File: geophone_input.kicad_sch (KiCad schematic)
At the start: 6 parts, among them J4 Conn_01x03_Socket

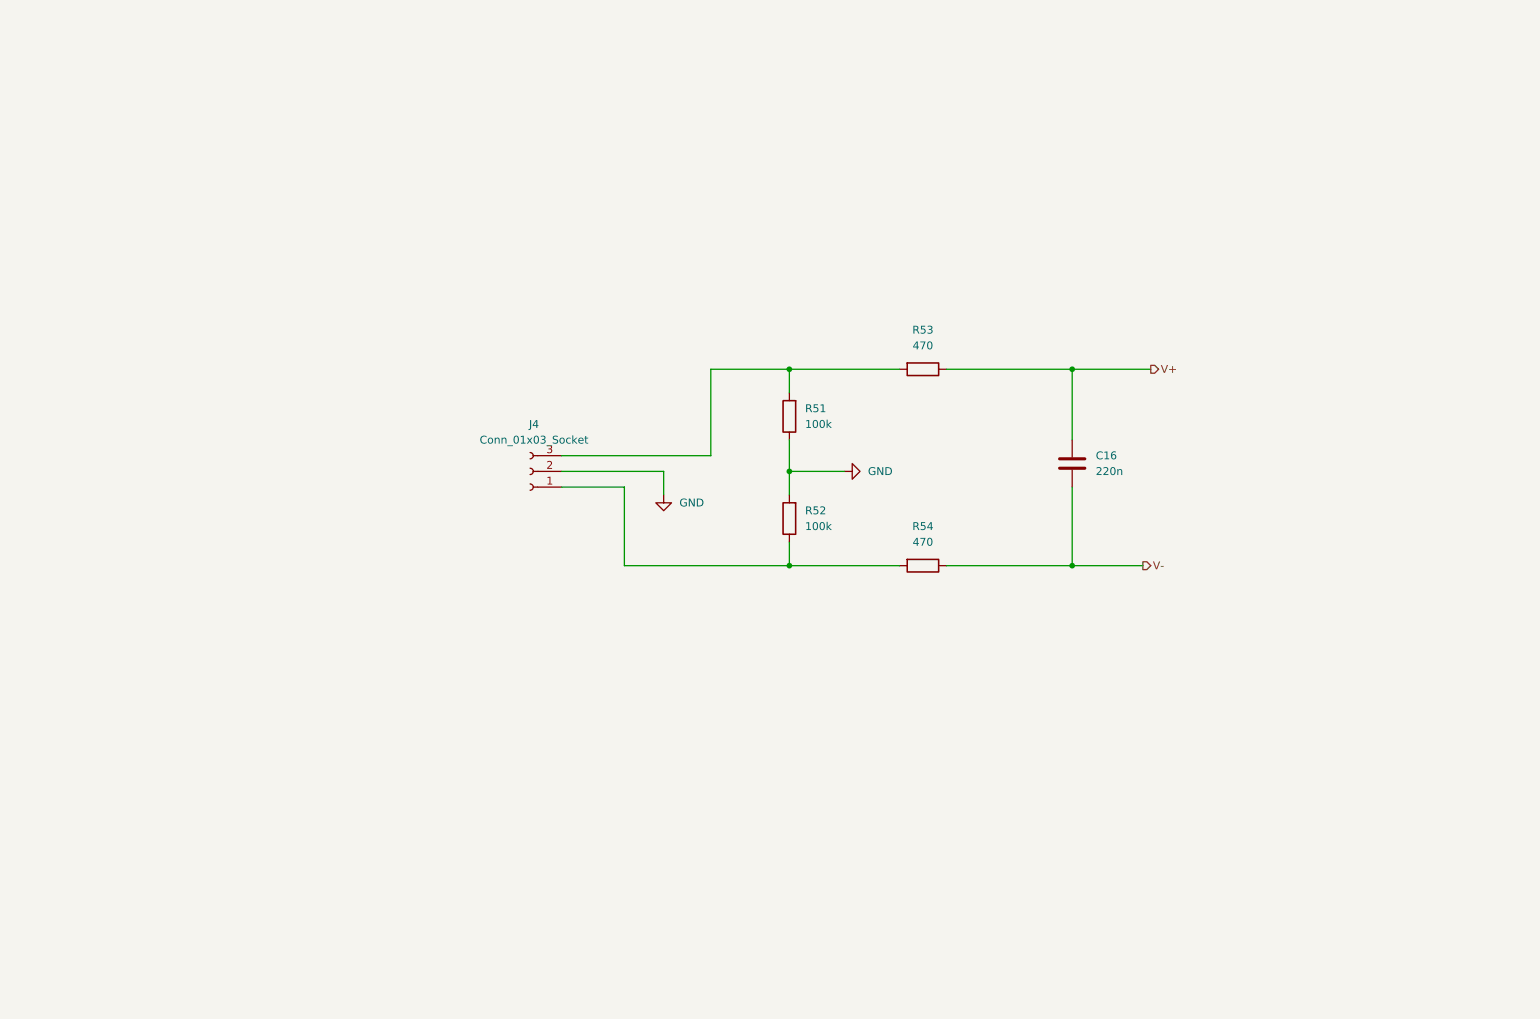
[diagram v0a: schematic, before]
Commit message: Active input filter
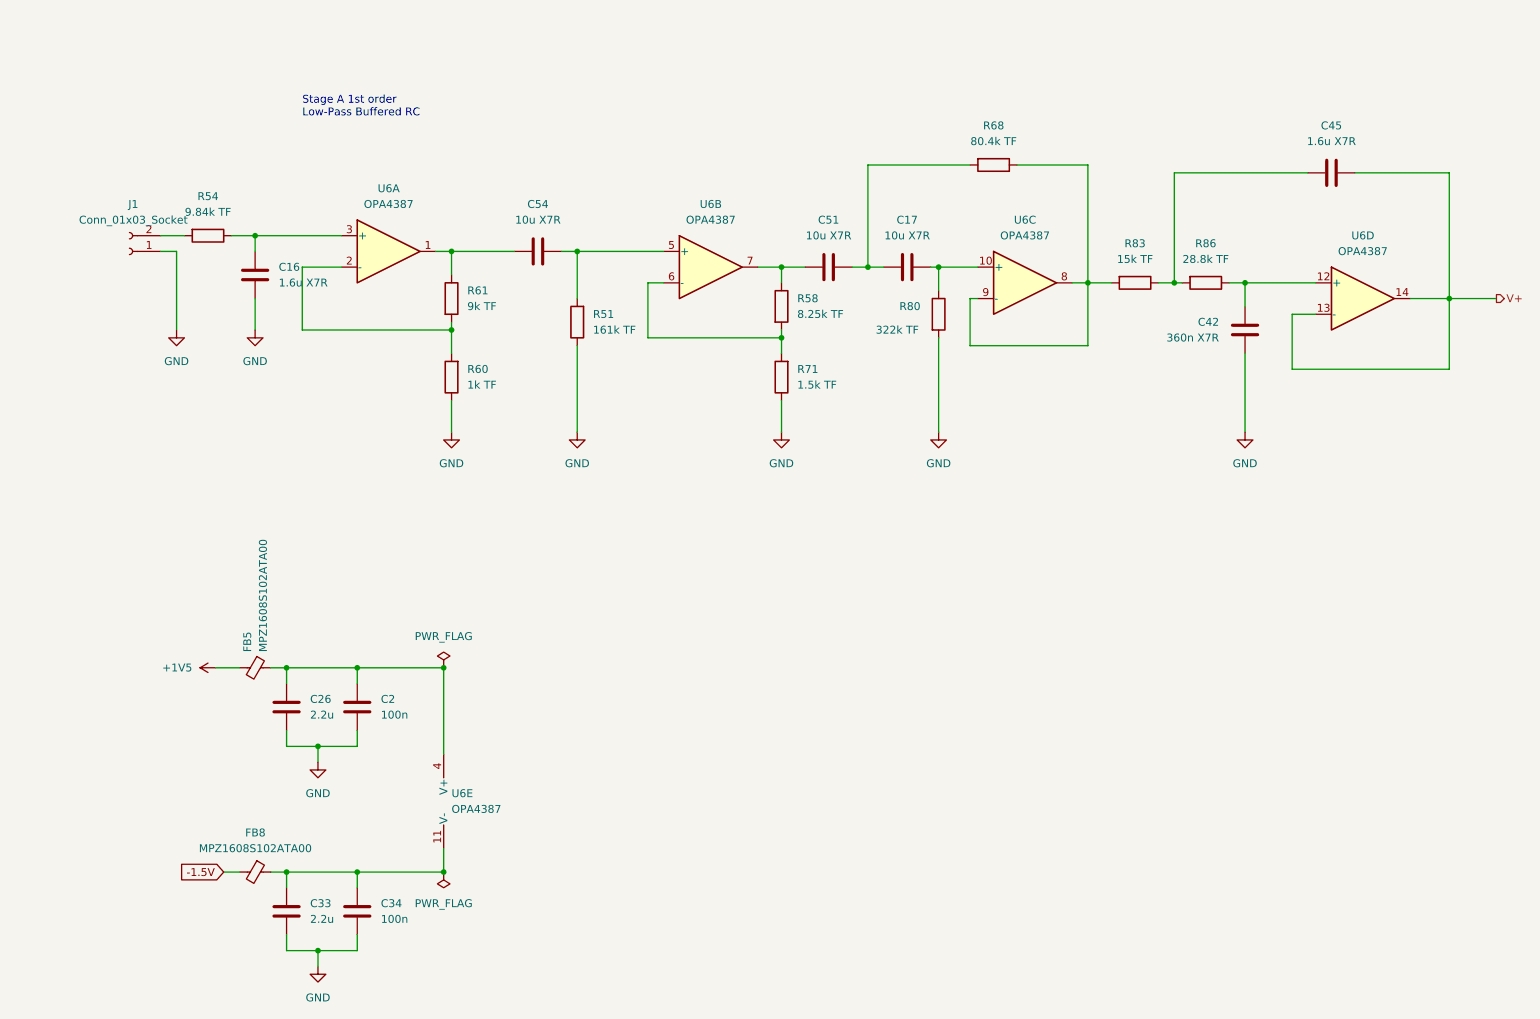
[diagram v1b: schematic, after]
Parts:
- removed J4: Conn_01x03_Socket, Connector_PinHeader_2.54mm:PinHeader_1x03_P2.54mm_Horizontal, symbol Connector:Conn_01x03_Socket
- removed R52: 100k, Resistor_SMD:R_0603_1608Metric, symbol Device:R
- removed R53: 470, Resistor_SMD:R_0603_1608Metric, symbol Device:R
- added C17, C51, C54: 10u X7R, Capacitor_SMD:C_0805_2012Metric_Pad1.18x1.45mm_HandSolder, symbol Device:C
- added C2, C34: 100n, Capacitor_SMD:C_0603_1608Metric_Pad1.08x0.95mm_HandSolder, symbol Device:C
- added C26, C33: 2.2u, Capacitor_SMD:C_0805_2012Metric, symbol Device:C
- added C42: 360n X7R, Capacitor_SMD:C_0805_2012Metric_Pad1.18x1.45mm_HandSolder, symbol Device:C
- added C45: 1.6u X7R, Capacitor_SMD:C_0805_2012Metric_Pad1.18x1.45mm_HandSolder, symbol Device:C
- added FB5, FB8: MPZ1608S102ATA00, Inductor_SMD:L_0805_2012Metric, symbol Device:FerriteBead_Small
- added J1: Conn_01x03_Socket, Connector_PinHeader_2.54mm:PinHeader_1x03_P2.54mm_Horizontal, symbol Connector:Conn_01x02_Socket
- added R58: 8.25k TF, Resistor_SMD:R_0603_1608Metric_Pad0.98x0.95mm_HandSolder, symbol Device:R
- added R60: 1k TF, Resistor_SMD:R_0603_1608Metric_Pad0.98x0.95mm_HandSolder, symbol Device:R
- added R61: 9k TF, Resistor_SMD:R_0603_1608Metric_Pad0.98x0.95mm_HandSolder, symbol Device:R
- added R68: 80.4k TF, Resistor_SMD:R_0603_1608Metric_Pad0.98x0.95mm_HandSolder, symbol Device:R
- added R71: 1.5k TF, Resistor_SMD:R_0603_1608Metric_Pad0.98x0.95mm_HandSolder, symbol Device:R
- added R80: 322k TF, Resistor_SMD:R_0603_1608Metric_Pad0.98x0.95mm_HandSolder, symbol Device:R
- added R83: 15k TF, Resistor_SMD:R_0603_1608Metric_Pad0.98x0.95mm_HandSolder, symbol Device:R
- added R86: 28.8k TF, Resistor_SMD:R_0603_1608Metric_Pad0.98x0.95mm_HandSolder, symbol Device:R
- added U6: OPA4387, Package_SO:TSSOP-14_4.4x5mm_P0.65mm, symbol seismometer:OPA4387
- C16: value 220n -> 1.6u X7R; footprint Capacitor_SMD:C_0603_1608Metric_Pad1.08x0.95mm_HandSolder -> Capacitor_SMD:C_0805_2012Metric_Pad1.18x1.45mm_HandSolder; MANUFACTURER TDK -> YAEGO; MP CGA3E3X7R1H224K080AB -> CC0402KRX5R6BB105
- R51: value 100k -> 161k TF; footprint Resistor_SMD:R_0603_1608Metric -> Resistor_SMD:R_0603_1608Metric_Pad0.98x0.95mm_HandSolder
- R54: value 470 -> 9.84k TF; footprint Resistor_SMD:R_0603_1608Metric -> Resistor_SMD:R_0603_1608Metric_Pad0.98x0.95mm_HandSolder; MP CRCW0603470RFKEA. -> CRCW0603100KFKEA
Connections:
- net GND: now also C16.2, C2.1, C26.1, C33.1, C34.1, C42.2, J1.1 (Pin_1), R60.1, R71.1, R80.2
- net V+: now also C45.2, U6.13 (-), U6.14; no longer C16.1
- net at R51.2: now also C54.2, U6.5 (+)
- net at R54.2: now also J1.2 (Pin_2)
- net V-: no longer names the net of R54.1
- net V-: now also C16.1, U6.3 (+); no longer C16.2
- new net: R60.2, R61.2, U6.2 (-)
- new net: R68.1, R83.2, U6.8, U6.9 (-)
- new net: C17.2, C51.1, R68.2
- new net: C54.1, R61.1, U6.1
- new net: C17.1, R80.1, U6.10 (+)
- new net: R58.2, R71.2, U6.6 (-)
- new net: C33.2, C34.2, FB8.1, U6.11 (V-)
- new net: C42.1, R86.1, U6.12 (+)
- new net: C45.1, R83.1, R86.2
- new net: C51.2, R58.1, U6.7
- new net: C2.2, C26.2, FB5.1, U6.4 (V+)
- new net +1V5: FB5.2
- new net -1.5V: FB8.2
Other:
- note added: "Stage A 1st order Low-Pass Buffered RC"

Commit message: wip Layout
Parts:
- C16, C17, C45, C51, C54: footprint Capacitor_SMD:C_0805_2012Metric_Pad1.18x1.45mm_HandSolder -> Capacitor_SMD:C_1206_3216Metric
- C26, C33: footprint Capacitor_SMD:C_0805_2012Metric -> Capacitor_SMD:C_1206_3216Metric
- J1: symbol Connector:Conn_01x02_Socket -> Connector:Conn_01x03_Socket
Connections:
- net GND: now also J1.3 (Pin_3)
- net at C51.1, R68.2: now also C17.1; no longer C17.2
- net at R80.1, U6.10 (+): now also C17.2; no longer C17.1
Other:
- note added: "1st order 0.1 Hz HP 6.5x gain"
- note added: "1st order 10 Hz LP 10x gain"
- note added: "2nd order 0.1 Hz sallen key HP Unity gain"
- note added: "2nd order 10 Hz sallen key LP Unity gain"
- note removed: "Stage A 1st order Low-Pass Buffered RC"
- moved on the sheet: C17
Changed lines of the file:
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@@
   (junction (at 67.31 161.29) (diameter 0) (color 0 0 0 0)
   )
+  (junction (at 31.75 60.96) (diameter 0) (color 0 0 0 0)
+  )
+  (wire (pts (xy 31.75 55.88) (xy 31.75 60.96))
+    (stroke (width 0) (type default))
+  )
   (wire (pts (xy 53.34 128.27) (xy 55.88 128.27))
     (stroke (width 0) (type default))
@@
     (stroke (width 0) (type default))
   )
+  (wire (pts (xy 31.75 60.96) (xy 31.75 73.66))
+    (stroke (width 0) (type default))
+  )
   (wire (pts (xy 82.55 60.96) (xy 92.71 60.96))
     (stroke (width 0) (type default))
@@
     (stroke (width 0) (type default))
   )
-  (wire (pts (xy 35.56 60.96) (xy 38.1 60.96))
-    (stroke (width 0) (type default))
-  )
   (wire (pts (xy 161.29 74.93) (xy 161.29 90.17))
     (stroke (width 0) (type default))
@@
     (stroke (width 0) (type default))
   )
+  (wire (pts (xy 26.67 55.88) (xy 31.75 55.88))
+    (stroke (width 0) (type default))
+  )
   (wire (pts (xy 55.88 138.43) (xy 55.88 140.97))
     (stroke (width 0) (type default))
@@
     (stroke (width 0) (type default))
   )
-  (wire (pts (xy 35.56 58.42) (xy 39.37 58.42))
-    (stroke (width 0) (type default))
-  )
   (wire (pts (xy 243.84 68.58) (xy 243.84 48.26))
     (stroke (width 0) (type default))
@@
     (stroke (width 0) (type default))
   )
+  (wire (pts (xy 26.67 58.42) (xy 39.37 58.42))
+    (stroke (width 0) (type default))
+  )
   (wire (pts (xy 44.45 128.27) (xy 48.26 128.27))
     (stroke (width 0) (type default))
@@
     (stroke (width 0) (type default))
   )
+  (wire (pts (xy 26.67 60.96) (xy 31.75 60.96))
+    (stroke (width 0) (type default))
+  )
   (wire (pts (xy 160.02 63.5) (xy 161.29 63.5))
     (stroke (width 0) (type default))
@@
     (stroke (width 0) (type default))
   )
-  (wire (pts (xy 38.1 60.96) (xy 38.1 73.66))
-    (stroke (width 0) (type default))
-  )
   (wire (pts (xy 55.88 173.99) (xy 60.96 173.99))
     (stroke (width 0) (type default))
@@
     (stroke (width 0) (type default))
   )
-  (text "Stage A 1st order\nLow-Pass Buffered RC " (at 58.42 39.37 0)
+  (text "2nd order 0.1 Hz sallen key HP\nUnity gain" (at 151.13 26.67 0)
+    (effects (font (size 1.27 1.27)) (justify left bottom))
+  )
+  (text "1st order 10 Hz LP\n10x gain" (at 64.77 29.21 0)
+    (effects (font (size 1.27 1.27)) (justify left bottom))
+  )
+  (text "1st order 0.1 Hz HP\n6.5x gain" (at 106.68 26.67 0)
+    (effects (font (size 1.27 1.27)) (justify left bottom))
+  )
+  (text "2nd order 10 Hz sallen key LP\nUnity gain" (at 200.66 26.67 0)
     (effects (font (size 1.27 1.27)) (justify left bottom))
   )
@@
     )
   )
-  (symbol (lib_id "power:GND") (at 38.1 73.66 0) (unit 1)
-    (in_bom yes) (on_board yes) (dnp no) (fields_autoplaced)
-    (property "Reference" "#PWR045" (at 38.1 80.01 0)
-      (effects (font (size 1.27 1.27)) hide)
-    )
-    (property "Value" "GND" (at 38.1 78.74 0)
-      (effects (font (size 1.27 1.27)))
-    )
-    (property "Footprint" "" (at 38.1 73.66 0)
-      (effects (font (size 1.27 1.27)) hide)
-    )
-    (property "Datasheet" "" (at 38.1 73.66 0)
+  (symbol (lib_id "power:GND") (at 31.75 73.66 0) (unit 1)
+    (in_bom yes) (on_board yes) (dnp no) (fields_autoplaced)
+    (property "Reference" "#PWR045" (at 31.75 80.01 0)
+      (effects (font (size 1.27 1.27)) hide)
+    )
+    (property "Value" "GND" (at 31.75 78.74 0)
+      (effects (font (size 1.27 1.27)))
+    )
+    (property "Footprint" "" (at 31.75 73.66 0)
+      (effects (font (size 1.27 1.27)) hide)
+    )
+    (property "Datasheet" "" (at 31.75 73.66 0)
       (effects (font (size 1.27 1.27)) hide)
     )
@@
     )
   )
-  (symbol (lib_id "Device:C") (at 156.21 63.5 270) (unit 1)
-    (in_bom yes) (on_board yes) (dnp no) (fields_autoplaced)
+  (symbol (lib_id "Device:C") (at 156.21 63.5 90) (mirror x) (unit 1)
+    (in_bom yes) (on_board yes) (dnp no)
     (property "Reference" "C17" (at 156.21 55.88 90)
       (effects (font (size 1.27 1.27)))
@@
       (effects (font (size 1.27 1.27)))
     )
-    (property "Footprint" "Capacitor_SMD:C_0805_2012Metric_Pad1.18x1.45mm_HandSolder" (at 152.4 64.4652 0)
+    (property "Footprint" "Capacitor_SMD:C_1206_3216Metric" (at 160.02 64.4652 0)
       (effects (font (size 1.27 1.27)) hide)
     )
@@
       (effects (font (size 1.27 1.27)) (justify left))
     )
-    (property "Footprint" "Capacitor_SMD:C_0805_2012Metric_Pad1.18x1.45mm_HandSolder" (at 51.7652 68.58 0)
+    (property "Footprint" "Capacitor_SMD:C_1206_3216Metric" (at 51.7652 68.58 0)
       (effects (font (size 1.27 1.27)) hide)
     )
@@
       (effects (font (size 1.27 1.27)))
     )
-    (property "Footprint" "Capacitor_SMD:C_0805_2012Metric_Pad1.18x1.45mm_HandSolder" (at 100.33 59.9948 0)
+    (property "Footprint" "Capacitor_SMD:C_1206_3216Metric" (at 100.33 59.9948 0)
       (effects (font (size 1.27 1.27)) hide)
     )
@@
     )
   )
-  (symbol (lib_id "Connector:Conn_01x02_Socket") (at 30.48 60.96 180) (unit 1)
-    (in_bom yes) (on_board yes) (dnp no) (fields_autoplaced)
-    (property "Reference" "J1" (at 31.115 53.34 0)
-      (effects (font (size 1.27 1.27)))
-    )
-    (property "Value" "Conn_01x03_Socket" (at 31.115 55.88 0)
-      (effects (font (size 1.27 1.27)))
-    )
-    (property "Footprint" "Connector_PinHeader_2.54mm:PinHeader_1x03_P2.54mm_Horizontal" (at 30.48 60.96 0)
-      (effects (font (size 1.27 1.27)) hide)
-    )
-    (property "Datasheet" "~" (at 30.48 60.96 0)
-      (effects (font (size 1.27 1.27)) hide)
-    )
-    (property "Description" "2.54mm right angle pin headers" (at 30.48 60.96 0)
-      (effects (font (size 1.27 1.27)) hide)
-    )
-    (property "MANUFACTURER" "MOLEX" (at 30.48 60.96 0)
-      (effects (font (size 1.27 1.27)) hide)
-    )
-    (property "MP" "22-12-4032" (at 30.48 60.96 0)
-      (effects (font (size 1.27 1.27)) hide)
-    )
-    (pin "1")
-    (pin "2")
+  (symbol (lib_id "Connector:Conn_01x03_Socket") (at 21.59 58.42 180) (unit 1)
+    (in_bom yes) (on_board yes) (dnp no) (fields_autoplaced)
+    (property "Reference" "J1" (at 22.225 50.8 0)
+      (effects (font (size 1.27 1.27)))
+    )
+    (property "Value" "Conn_01x03_Socket" (at 22.225 53.34 0)
+      (effects (font (size 1.27 1.27)))
+    )
+    (property "Footprint" "Connector_PinHeader_2.54mm:PinHeader_1x03_P2.54mm_Horizontal" (at 21.59 58.42 0)
+      (effects (font (size 1.27 1.27)) hide)
+    )
+    (property "Datasheet" "~" (at 21.59 58.42 0)
+      (effects (font (size 1.27 1.27)) hide)
+    )
+    (property "Description" "2.54mm right angle pin headers" (at 21.59 58.42 0)
+      (effects (font (size 1.27 1.27)) hide)
+    )
+    (property "MANUFACTURER" "MOLEX" (at 21.59 58.42 0)
+      (effects (font (size 1.27 1.27)) hide)
+    )
+    (property "MP" "22-12-4032" (at 21.59 58.42 0)
+      (effects (font (size 1.27 1.27)) hide)
+    )
+    (pin "1")
+    (pin "2")
+    (pin "3")
     (instances
       (project "Seismometer"
@@
       (effects (font (size 1.27 1.27)))
     )
-    (property "Footprint" "Capacitor_SMD:C_0805_2012Metric_Pad1.18x1.45mm_HandSolder" (at 139.7 64.4652 0)
+    (property "Footprint" "Capacitor_SMD:C_1206_3216Metric" (at 139.7 64.4652 0)
       (effects (font (size 1.27 1.27)) hide)
     )
@@
       (effects (font (size 1.27 1.27)))
     )
-    (property "Footprint" "Capacitor_SMD:C_0805_2012Metric_Pad1.18x1.45mm_HandSolder" (at 228.6 47.2948 0)
+    (property "Footprint" "Capacitor_SMD:C_1206_3216Metric" (at 228.6 47.2948 0)
       (effects (font (size 1.27 1.27)) hide)
     )
@@
       (effects (font (size 1.27 1.27)) (justify right))
     )
-    (property "Footprint" "Capacitor_SMD:C_0805_2012Metric" (at 54.9148 163.83 0)
+    (property "Footprint" "Capacitor_SMD:C_1206_3216Metric" (at 54.9148 163.83 0)
       (effects (font (size 1.27 1.27)) hide)
     )
@@
       (effects (font (size 1.27 1.27)) (justify right))
     )
-    (property "Footprint" "Capacitor_SMD:C_0805_2012Metric" (at 54.9148 130.81 0)
-      (effects (font (size 1.27 1.27)) hide)
-    )
+    (property "Footprint" "Capacitor_SMD:C_1206_3216Metric" (at 54.9148 130.81 0)
+      (effects (font (size 1.27 1.27)) hide)
+    )
